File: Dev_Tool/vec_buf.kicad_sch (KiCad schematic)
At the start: 1 part, among them U11 SN74HCT245DWR

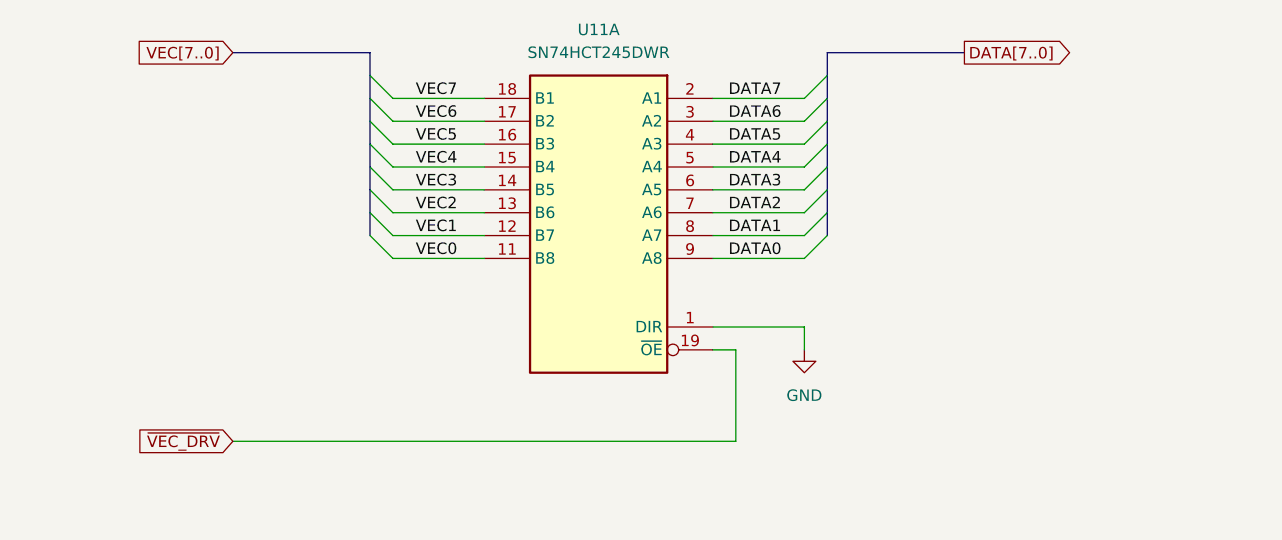
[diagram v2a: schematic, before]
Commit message: Rev 2 fixes
* R5/C1 reference silkscreens were swapped around
* LED logic for the PC LED was reverse to what I thought it would be, fixed by adding Q1
* Change DEV LED to PWR ON LED, since it comes on when the port is powered, not just when a device is connected. Switched via Q2 so it doesnt fade on power down.
* IN USE LED now comes off MCP2221A pin - the PCA9535 doesnt have a reset, so this LED could remain lit even after a reset.
* Pull up/down added to vector buffer
* 8P8C sockets moved further out as they are shorter than the footprint suggests
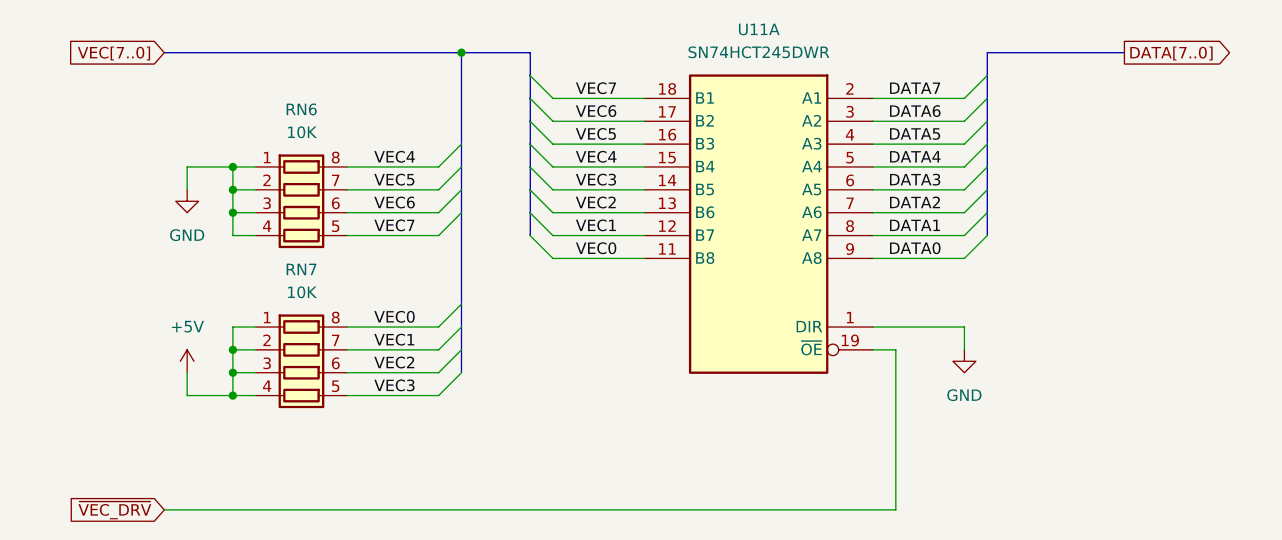
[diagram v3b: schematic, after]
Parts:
- added RN6, RN7: 10K, COMET_footprints:R_Cat16-4, symbol Device:R_Pack04
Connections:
- net GND: now also RN6.1 (R1.1), RN6.2 (R2.1), RN6.3 (R3.1), RN6.4 (R4.1)
- net VEC0: now also RN7.8 (R1.2)
- net VEC1: now also RN7.7 (R2.2)
- net VEC2: now also RN7.6 (R3.2)
- net VEC3: now also RN7.5 (R4.2)
- net VEC4: now also RN6.8 (R1.2)
- net VEC5: now also RN6.7 (R2.2)
- net VEC6: now also RN6.6 (R3.2)
- net VEC7: now also RN6.5 (R4.2)
- new net +5V: RN7.1 (R1.1), RN7.2 (R2.1), RN7.3 (R3.1), RN7.4 (R4.1)
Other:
- moved on the sheet: U11A
